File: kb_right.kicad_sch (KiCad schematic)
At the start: 171 parts, among them J1 10029449-001RLF, SW1 RotaryEncoder_Switch

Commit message: added footprints
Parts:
- C101, C102, C103, C104, C105, C106, C107, C108, C109, C110, C111, C112, C113, C114, C115, C116, C117, C118, C119, C120, C121, C122, C123, C124, C125, C126, C127, C128, C129, C130, C131, C132, C133, C134, C135, C136, C137, C138, C139, C140, C141, C142: footprint (none) -> Capacitor_SMD:C_0805_2012Metric_Pad1.18x1.45mm_HandSolder
- D1, D10, D11, D12, D13, D14, D15, D16, D17, D18, D19, D2, D20, D21, D22, D23, D24, D25, D26, D27, D28, D29, D3, D30, D31, D32, D33, D34, D35, D36, D37, D38, D39, D4, D40, D41, D42, D43, D5, D6, D7, D8: footprint (none) -> Diode_SMD:D_SOD-123
- D101, D102, D103, D104, D105, D106, D107, D108, D109, D110, D111, D112, D113, D114, D115, D116, D117, D118, D119, D120, D121, D122, D123, D124, D125, D126, D127, D128, D129, D130, D131, D132, D133, D134, D135, D136, D137, D138, D139, D140, D141, D142: footprint LED_SMD:LED_SK6812MINI_PLCC4_3.5x3.5mm_P1.75mm -> Keebio-Parts:SK6812-MINI-E
- MX1, MX10, MX11, MX12, MX13, MX14, MX15, MX17, MX18, MX19, MX2, MX20, MX21, MX22, MX23, MX25, MX26, MX27, MX28, MX29, MX3, MX30, MX31, MX33, MX34, MX4, MX40, MX41, MX42, MX5, MX6, MX8, MX9: footprint (none) -> MX_Only:MXOnly-1U-Hotswap
- MX16, MX35: footprint (none) -> MX_Only:MXOnly-1.5U-Hotswap
- MX24: footprint (none) -> MX_Only:MXOnly-2.25U-Hotswap
- MX32: footprint (none) -> MX_Only:MXOnly-2.75U-Hotswap
- MX36, MX37, MX38, MX39: footprint (none) -> MX_Only:MXOnly-1.25U-Hotswap
- MX7: footprint (none) -> MX_Only:MXOnly-2U-Hotswap

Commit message: laid out right keys
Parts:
- renumbered D9 to D0, D11 to D10, D12 to D11, D13 to D12, D14 to D13, D15 to D14, D16 to D15, D17 to D16, D18 to D17, D19 to D18, D20 to D19, D21 to D20, D22 to D21, D23 to D22, D24 to D23, D25 to D24, D26 to D25, D27 to D26, D28 to D27, D29 to D28, D30 to D29, D31 to D30, D32 to D31, D33 to D32, D34 to D33, D35 to D34, D36 to D35, D37 to D36, D38 to D37, D39 to D38, D40 to D39, D41 to D40, D42 to D41, D43 to D42, D10 to D9, SW1 to SW0

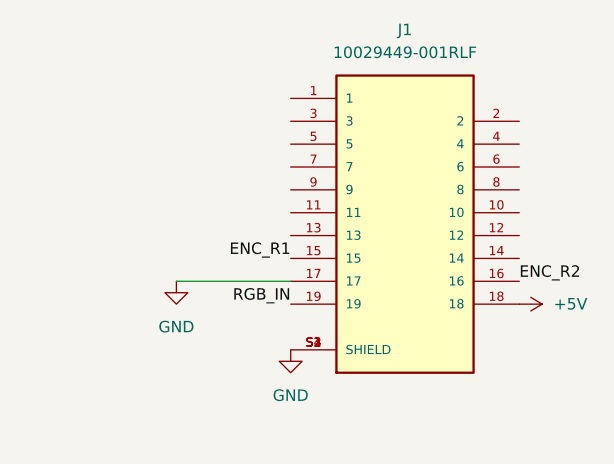
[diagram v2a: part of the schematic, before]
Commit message: labelled hdmi port
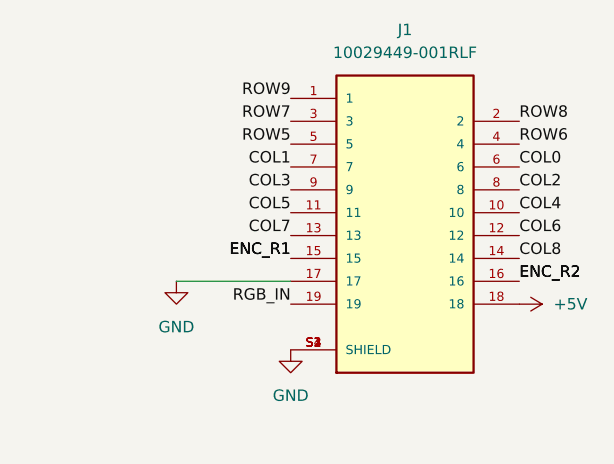
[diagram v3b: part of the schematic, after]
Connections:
- net COL0: now also J1.6
- net COL1: now also J1.7
- net COL2: now also J1.8
- net COL3: now also J1.9
- net COL4: now also J1.10
- net COL5: now also J1.11
- net COL6: now also J1.12
- net COL7: now also J1.13
- net COL8: now also J1.14
- net ROW5: now also J1.5
- net ROW6: now also J1.4
- net ROW7: now also J1.3
- net ROW8: now also J1.2
- net ROW9: now also J1.1
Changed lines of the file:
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@@
+    (effects (font (size 1.27 1.27)) (justify left bottom))
+  )
+  (label "COL0" (at 396.24 31.75 0)
     (effects (font (size 1.27 1.27)) (justify left bottom))
   )
@@
     (effects (font (size 1.27 1.27)) (justify right bottom))
   )
+  (label "ENC_R1" (at 370.84 41.91 180)
+    (effects (font (size 1.27 1.27)) (justify right bottom))
+  )
+  (label "COL4" (at 396.24 36.83 0)
+    (effects (font (size 1.27 1.27)) (justify left bottom))
+  )
   (label "COL2" (at 125.73 24.13 90)
+    (effects (font (size 1.27 1.27)) (justify left bottom))
+  )
+  (label "ROW9" (at 370.84 24.13 180)
+    (effects (font (size 1.27 1.27)) (justify right bottom))
+  )
+  (label "COL8" (at 396.24 41.91 0)
     (effects (font (size 1.27 1.27)) (justify left bottom))
   )
@@
   (label "ROW9" (at 30.48 168.91 180)
     (effects (font (size 1.27 1.27)) (justify right bottom))
+  )
+  (label "ROW8" (at 396.24 26.67 0)
+    (effects (font (size 1.27 1.27)) (justify left bottom))
   )
   (label "RGB_IN" (at 24.13 189.23 180)
@@
     (effects (font (size 1.27 1.27)) (justify left bottom))
   )
+  (label "ENC_R2" (at 396.24 44.45 0)
+    (effects (font (size 1.27 1.27)) (justify left bottom))
+  )
+  (label "ROW7" (at 370.84 26.67 180)
+    (effects (font (size 1.27 1.27)) (justify right bottom))
+  )
+  (label "COL5" (at 370.84 36.83 180)
+    (effects (font (size 1.27 1.27)) (justify right bottom))
+  )
   (label "COL1" (at 97.79 24.13 90)
     (effects (font (size 1.27 1.27)) (justify left bottom))
@@
   (label "ENC_R1" (at 273.05 33.02 180)
     (effects (font (size 1.27 1.27)) (justify right bottom))
+  )
+  (label "COL1" (at 370.84 31.75 180)
+    (effects (font (size 1.27 1.27)) (justify right bottom))
+  )
+  (label "COL7" (at 370.84 39.37 180)
+    (effects (font (size 1.27 1.27)) (justify right bottom))
+  )
+  (label "ROW6" (at 396.24 29.21 0)
+    (effects (font (size 1.27 1.27)) (justify left bottom))
+  )
+  (label "COL6" (at 396.24 39.37 0)
+    (effects (font (size 1.27 1.27)) (justify left bottom))
   )
   (label "ENC_R2" (at 396.24 44.45 0)
@@
     (effects (font (size 1.27 1.27)) (justify right bottom))
   )
+  (label "COL3" (at 370.84 34.29 180)
+    (effects (font (size 1.27 1.27)) (justify right bottom))
+  )
   (label "COL5" (at 208.28 24.13 90)
     (effects (font (size 1.27 1.27)) (justify left bottom))
   )
   (label "ENC_R1" (at 370.84 41.91 180)
+    (effects (font (size 1.27 1.27)) (justify right bottom))
+  )
+  (label "ROW5" (at 370.84 29.21 180)
     (effects (font (size 1.27 1.27)) (justify right bottom))
   )
@@
     (effects (font (size 1.27 1.27)) (justify left bottom))
   )
+  (label "COL2" (at 396.24 34.29 0)
+    (effects (font (size 1.27 1.27)) (justify left bottom))
+  )

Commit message: most routing done
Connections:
- net ENC_R1: now also J1.16; no longer J1.15
- net ENC_R2: now also J1.15; no longer J1.16
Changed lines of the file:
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@@
-    (effects (font (size 1.27 1.27)) (justify right bottom))
-  )
-  (label "ENC_R1" (at 370.84 41.91 180)
     (effects (font (size 1.27 1.27)) (justify right bottom))
   )
@@
   (label "ROW9" (at 370.84 24.13 180)
     (effects (font (size 1.27 1.27)) (justify right bottom))
+  )
+  (label "ENC_R1" (at 396.24 44.45 0)
+    (effects (font (size 1.27 1.27)) (justify left bottom))
   )
   (label "COL8" (at 396.24 41.91 0)
@@
     (effects (font (size 1.27 1.27)) (justify left bottom))
   )
-  (label "ENC_R2" (at 396.24 44.45 0)
-    (effects (font (size 1.27 1.27)) (justify left bottom))
-  )
   (label "ROW7" (at 370.84 26.67 180)
     (effects (font (size 1.27 1.27)) (justify right bottom))
@@
     (effects (font (size 1.27 1.27)) (justify right bottom))
   )
+  (label "ENC_R2" (at 370.84 41.91 180)
+    (effects (font (size 1.27 1.27)) (justify right bottom))
+  )
   (label "COL1" (at 370.84 31.75 180)
     (effects (font (size 1.27 1.27)) (justify right bottom))
@@
   )
   (label "COL6" (at 396.24 39.37 0)
-    (effects (font (size 1.27 1.27)) (justify left bottom))
-  )
-  (label "ENC_R2" (at 396.24 44.45 0)
     (effects (font (size 1.27 1.27)) (justify left bottom))
   )
@@
     (effects (font (size 1.27 1.27)) (justify left bottom))
   )
-  (label "ENC_R1" (at 370.84 41.91 180)
-    (effects (font (size 1.27 1.27)) (justify right bottom))
-  )
   (label "ROW5" (at 370.84 29.21 180)

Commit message: tearing up tracks to fix sk6812
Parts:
- D101, D102, D103, D104, D105, D106, D107, D108, D109, D110, D111, D112, D113, D114, D115, D116, D117, D118, D119, D120, D121, D122, D123, D124, D125, D126, D127, D128, D129, D130, D131, D132, D133, D134, D135, D136, D137, D138, D139, D140, D141, D142: symbol LED:SK6812MINI -> LED:WS2812B
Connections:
- net +5V: now also D101.1 (VDD), D102.1 (VDD), D103.1 (VDD), D104.1 (VDD), D105.1 (VDD), D106.1 (VDD), D107.1 (VDD), D108.1 (VDD), D109.1 (VDD), D110.1 (VDD), D111.1 (VDD), D112.1 (VDD), D113.1 (VDD), D114.1 (VDD), D115.1 (VDD), D116.1 (VDD), D117.1 (VDD), D118.1 (VDD), D119.1 (VDD), D120.1 (VDD), D121.1 (VDD), D122.1 (VDD), D123.1 (VDD), D124.1 (VDD), D125.1 (VDD), D126.1 (VDD), D127.1 (VDD), D128.1 (VDD), D129.1 (VDD), D130.1 (VDD), D131.1 (VDD), D132.1 (VDD), D133.1 (VDD), D134.1 (VDD), D135.1 (VDD), D136.1 (VDD), D137.1 (VDD), D138.1 (VDD), D139.1 (VDD), D140.1 (VDD), D141.1 (VDD), D142.1 (VDD); no longer D101.4 (VDD), D102.4 (VDD), D103.4 (VDD), D104.4 (VDD), D105.4 (VDD), D106.4 (VDD), D107.4 (VDD), D108.4 (VDD), D109.4 (VDD), D110.4 (VDD), D111.4 (VDD), D112.4 (VDD), D113.4 (VDD), D114.4 (VDD), D115.4 (VDD), D116.4 (VDD), D117.4 (VDD), D118.4 (VDD), D119.4 (VDD), D120.4 (VDD), D121.4 (VDD), D122.4 (VDD), D123.4 (VDD), D124.4 (VDD), D125.4 (VDD), D126.4 (VDD), D127.4 (VDD), D128.4 (VDD), D129.4 (VDD), D130.4 (VDD), D131.4 (VDD), D132.4 (VDD), D133.4 (VDD), D134.4 (VDD), D135.4 (VDD), D136.4 (VDD), D137.4 (VDD), D138.4 (VDD), D139.4 (VDD), D140.4 (VDD), D141.4 (VDD), D142.4 (VDD)
- net GND: now also D101.3 (VSS), D102.3 (VSS), D103.3 (VSS), D104.3 (VSS), D105.3 (VSS), D106.3 (VSS), D107.3 (VSS), D108.3 (VSS), D109.3 (VSS), D110.3 (VSS), D111.3 (VSS), D112.3 (VSS), D113.3 (VSS), D114.3 (VSS), D115.3 (VSS), D116.3 (VSS), D117.3 (VSS), D118.3 (VSS), D119.3 (VSS), D120.3 (VSS), D121.3 (VSS), D122.3 (VSS), D123.3 (VSS), D124.3 (VSS), D125.3 (VSS), D126.3 (VSS), D127.3 (VSS), D128.3 (VSS), D129.3 (VSS), D130.3 (VSS), D131.3 (VSS), D132.3 (VSS), D133.3 (VSS), D134.3 (VSS), D135.3 (VSS), D136.3 (VSS), D137.3 (VSS), D138.3 (VSS), D139.3 (VSS), D140.3 (VSS), D141.3 (VSS), D142.3 (VSS); no longer D101.2 (VSS), D102.2 (VSS), D103.2 (VSS), D104.2 (VSS), D105.2 (VSS), D106.2 (VSS), D107.2 (VSS), D108.2 (VSS), D109.2 (VSS), D110.2 (VSS), D111.2 (VSS), D112.2 (VSS), D113.2 (VSS), D114.2 (VSS), D115.2 (VSS), D116.2 (VSS), D117.2 (VSS), D118.2 (VSS), D119.2 (VSS), D120.2 (VSS), D121.2 (VSS), D122.2 (VSS), D123.2 (VSS), D124.2 (VSS), D125.2 (VSS), D126.2 (VSS), D127.2 (VSS), D128.2 (VSS), D129.2 (VSS), D130.2 (VSS), D131.2 (VSS), D132.2 (VSS), D133.2 (VSS), D134.2 (VSS), D135.2 (VSS), D136.2 (VSS), D137.2 (VSS), D138.2 (VSS), D139.2 (VSS), D140.2 (VSS), D141.2 (VSS), D142.2 (VSS)
- net RGB_IN: now also D101.4 (DIN); no longer D101.3 (DIN)
- new net: D106.2 (DOUT), D107.4 (DIN)
- new net: D105.2 (DOUT), D106.4 (DIN)
- new net: D141.2 (DOUT), D142.4 (DIN)
- new net: D108.2 (DOUT), D109.4 (DIN)
- new net: D107.2 (DOUT), D108.4 (DIN)
- new net: D140.2 (DOUT), D141.4 (DIN)
- new net: D129.2 (DOUT), D130.4 (DIN)
- new net: D128.2 (DOUT), D129.4 (DIN)
- new net: D114.2 (DOUT), D115.4 (DIN)
- new net: D113.2 (DOUT), D114.4 (DIN)
- new net: D121.2 (DOUT), D122.4 (DIN)
- new net: D120.2 (DOUT), D121.4 (DIN)
- new net: D132.2 (DOUT), D133.4 (DIN)
- new net: D131.2 (DOUT), D132.4 (DIN)
- new net: D117.2 (DOUT), D118.4 (DIN)
- new net: D116.2 (DOUT), D117.4 (DIN)
- new net: D104.2 (DOUT), D105.4 (DIN)
- new net: D103.2 (DOUT), D104.4 (DIN)
- new net: D127.2 (DOUT), D128.4 (DIN)
- new net: D126.2 (DOUT), D127.4 (DIN)
- new net: D102.2 (DOUT), D103.4 (DIN)
- new net: D134.2 (DOUT), D135.4 (DIN)
- new net: D133.2 (DOUT), D134.4 (DIN)
- new net: D122.2 (DOUT), D123.4 (DIN)
- new net: D130.2 (DOUT), D131.4 (DIN)
- new net: D119.2 (DOUT), D120.4 (DIN)
- new net: D118.2 (DOUT), D119.4 (DIN)
- new net: D123.2 (DOUT), D124.4 (DIN)
- new net: D115.2 (DOUT), D116.4 (DIN)
- new net: D109.2 (DOUT), D110.4 (DIN)
- new net: D125.2 (DOUT), D126.4 (DIN)
- new net: D124.2 (DOUT), D125.4 (DIN)
- new net: D139.2 (DOUT), D140.4 (DIN)
- new net: D112.2 (DOUT), D113.4 (DIN)
- new net: D111.2 (DOUT), D112.4 (DIN)
- new net: D101.2 (DOUT), D102.4 (DIN)
- new net: D138.2 (DOUT), D139.4 (DIN)
- new net: D137.2 (DOUT), D138.4 (DIN)
- new net: D136.2 (DOUT), D137.4 (DIN)
- new net: D135.2 (DOUT), D136.4 (DIN)
- new net: D110.2 (DOUT), D111.4 (DIN)

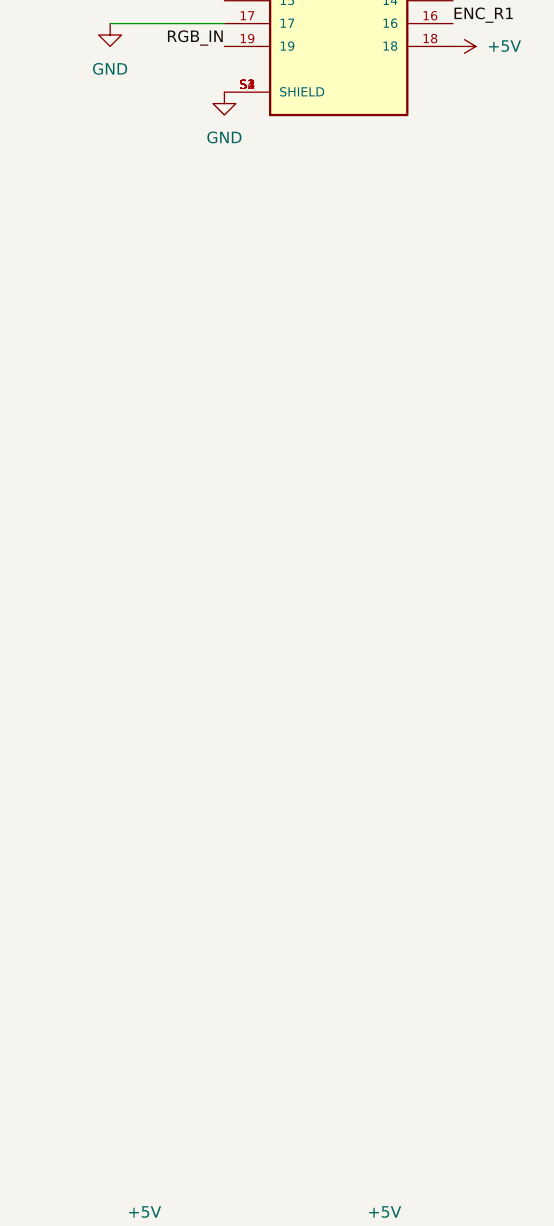
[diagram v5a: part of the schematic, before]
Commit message: add test points
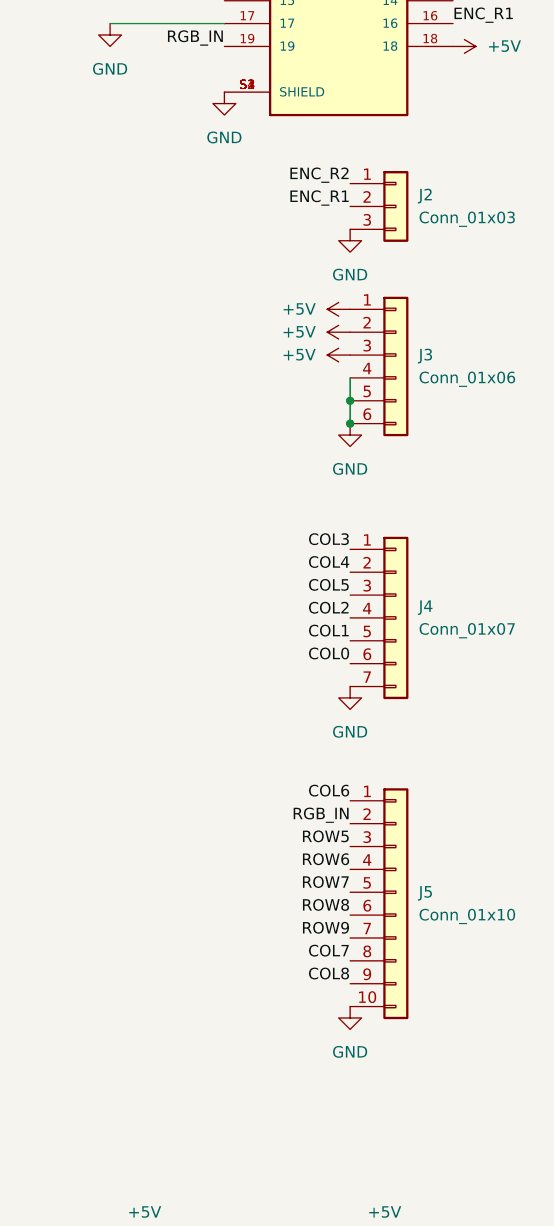
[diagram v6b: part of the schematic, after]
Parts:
- added J2: Conn_01x03, Connector_PinHeader_2.54mm:PinHeader_1x03_P2.54mm_Vertical, symbol Connector_Generic:Conn_01x03
- added J3: Conn_01x06, Connector_PinHeader_2.54mm:PinHeader_1x06_P2.54mm_Vertical, symbol Connector_Generic:Conn_01x06
- added J4: Conn_01x07, Connector_PinHeader_2.54mm:PinHeader_1x07_P2.54mm_Vertical, symbol Connector_Generic:Conn_01x07
- added J5: Conn_01x10, Connector_PinHeader_2.54mm:PinHeader_1x10_P2.54mm_Vertical, symbol Connector_Generic:Conn_01x10
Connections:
- net +5V: now also J3.1 (Pin_1), J3.2 (Pin_2), J3.3 (Pin_3)
- net COL0: now also J4.6 (Pin_6)
- net COL1: now also J4.5 (Pin_5)
- net COL2: now also J4.4 (Pin_4)
- net COL3: now also J4.1 (Pin_1)
- net COL4: now also J4.2 (Pin_2)
- net COL5: now also J4.3 (Pin_3)
- net COL6: now also J5.1 (Pin_1)
- net COL7: now also J5.8 (Pin_8)
- net COL8: now also J5.9 (Pin_9)
- net ENC_R1: now also J2.2 (Pin_2)
- net ENC_R2: now also J2.1 (Pin_1)
- net GND: now also J2.3 (Pin_3), J3.4 (Pin_4), J3.5 (Pin_5), J3.6 (Pin_6), J4.7 (Pin_7), J5.10 (Pin_10)
- net RGB_IN: now also J5.2 (Pin_2)
- net ROW5: now also J5.3 (Pin_3)
- net ROW6: now also J5.4 (Pin_4)
- net ROW7: now also J5.5 (Pin_5)
- net ROW8: now also J5.6 (Pin_6)
- net ROW9: now also J5.7 (Pin_7)

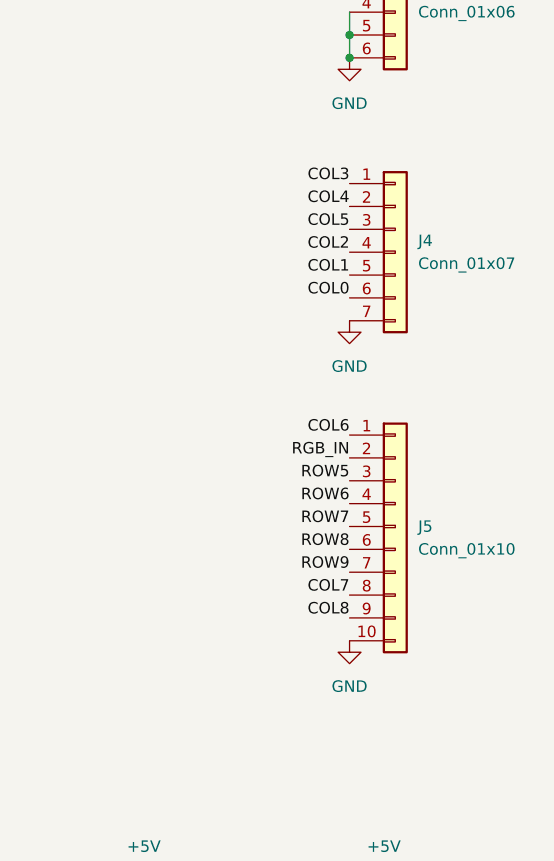
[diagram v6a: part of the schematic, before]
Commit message: add silkscreen
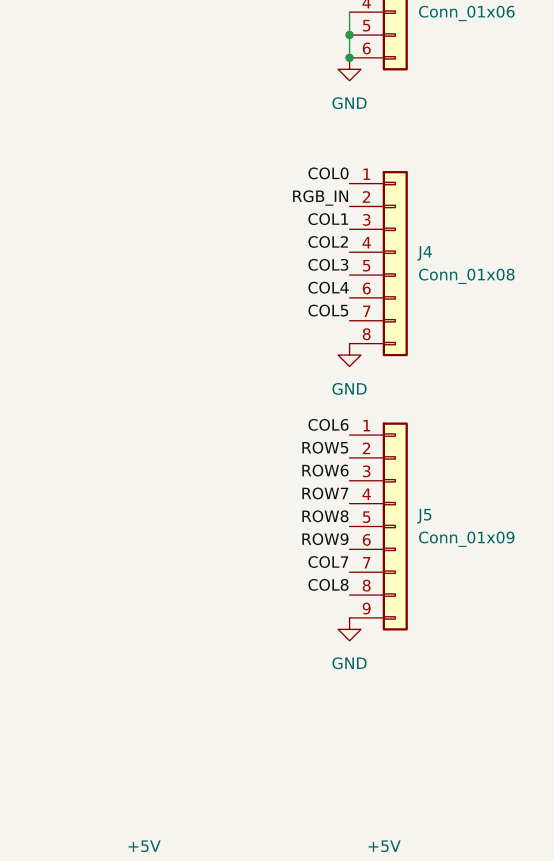
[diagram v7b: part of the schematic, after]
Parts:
- J4: value Conn_01x07 -> Conn_01x08; footprint Connector_PinHeader_2.54mm:PinHeader_1x07_P2.54mm_Vertical -> Connector_PinHeader_2.54mm:PinHeader_1x08_P2.54mm_Vertical; symbol Connector_Generic:Conn_01x07 -> Connector_Generic:Conn_01x08
- J5: value Conn_01x10 -> Conn_01x09; footprint Connector_PinHeader_2.54mm:PinHeader_1x10_P2.54mm_Vertical -> Connector_PinHeader_2.54mm:PinHeader_1x09_P2.54mm_Vertical; symbol Connector_Generic:Conn_01x10 -> Connector_Generic:Conn_01x09
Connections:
- net COL0: now also J4.1 (Pin_1); no longer J4.6 (Pin_6)
- net COL1: now also J4.3 (Pin_3); no longer J4.5 (Pin_5)
- net COL3: now also J4.5 (Pin_5); no longer J4.1 (Pin_1)
- net COL4: now also J4.6 (Pin_6); no longer J4.2 (Pin_2)
- net COL5: now also J4.7 (Pin_7); no longer J4.3 (Pin_3)
- net COL7: now also J5.7 (Pin_7); no longer J5.8 (Pin_8)
- net COL8: now also J5.8 (Pin_8); no longer J5.9 (Pin_9)
- net GND: now also J4.8 (Pin_8), J5.9 (Pin_9); no longer J4.7 (Pin_7), J5.10 (Pin_10)
- net RGB_IN: now also J4.2 (Pin_2); no longer J5.2 (Pin_2)
- net ROW5: now also J5.2 (Pin_2); no longer J5.3 (Pin_3)
- net ROW6: now also J5.3 (Pin_3); no longer J5.4 (Pin_4)
- net ROW7: now also J5.4 (Pin_4); no longer J5.5 (Pin_5)
- net ROW8: now also J5.5 (Pin_5); no longer J5.6 (Pin_6)
- net ROW9: now also J5.6 (Pin_6); no longer J5.7 (Pin_7)

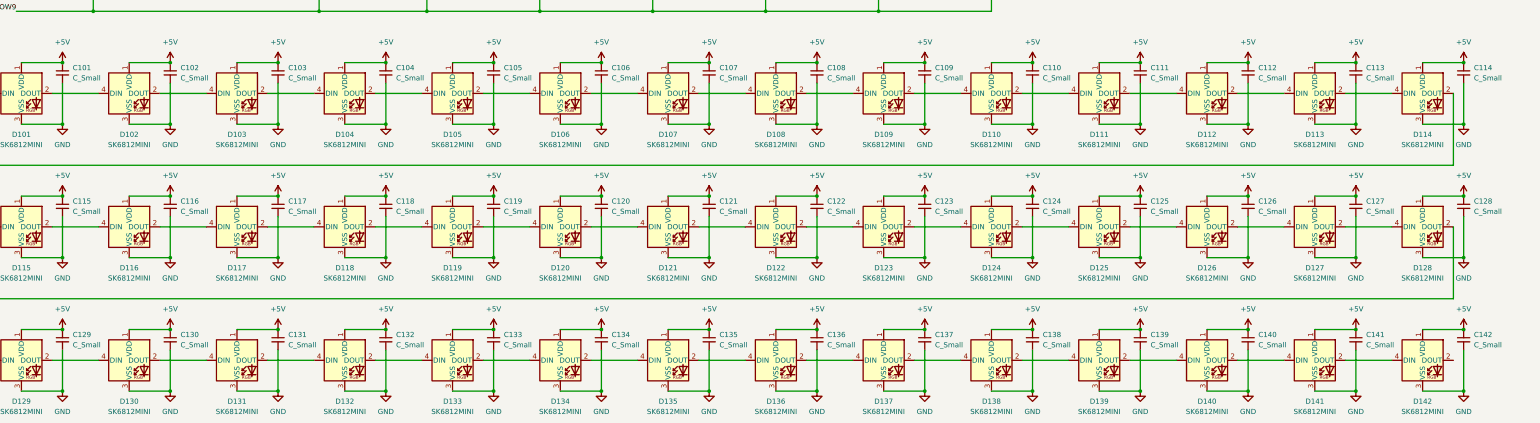
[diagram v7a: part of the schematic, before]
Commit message: change cap values
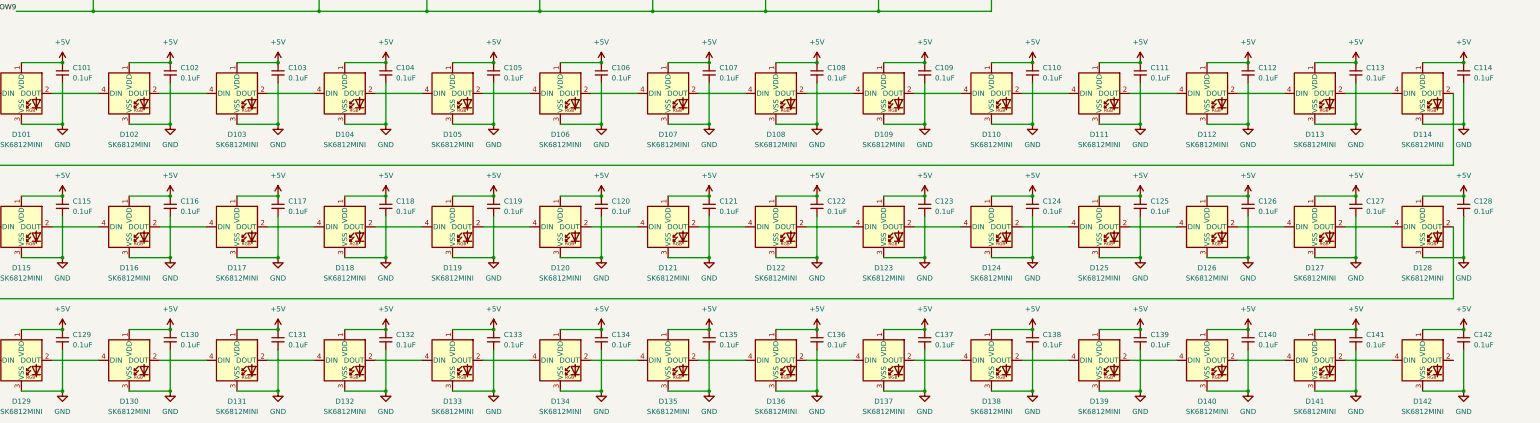
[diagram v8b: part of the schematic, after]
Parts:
- C101, C102, C103, C104, C105, C106, C107, C108, C109, C110, C111, C112, C113, C114, C115, C116, C117, C118, C119, C120, C121, C122, C123, C124, C125, C126, C127, C128, C129, C130, C131, C132, C133, C134, C135, C136, C137, C138, C139, C140, C141, C142: value C_Small -> 0.1uF
